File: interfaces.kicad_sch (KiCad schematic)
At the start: 87 parts, among them IC3 TPD8S009DSMR, J5 HDMI-A_685119134923, J6 USB_Micro-B_629105150521, J7 MicroSD_1140084168, Q3 BSS138PW, Q4 BSS138PW, Q5 BSS138PW, Q6 BSS138PW, Q7 BSS138PW, U10 FT4232H_QFN, Y2 Oscillator_SMD_12MHz_KX-7

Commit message: [#80386] Add company name in board settings
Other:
- company: Antmicro Ltd. -> Antmicro
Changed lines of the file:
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@@
 		(date "2023-07-27")
 		(rev "1.0.1")
-		(company "Antmicro Ltd.")
+		(company "Antmicro")
 		(comment 1 "www.antmicro.com")
-		(comment 2 "Antmicro Ltd")
 	)
 	(text "Debug USB"

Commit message: [#87036] Update components, clear DRC and ERC
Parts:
- removed IC3: TPD8S009DSMR, data-center-rdimm-ddr5-tester-footprints:R-PDSO-N15, symbol data-center-rdimm-ddr5-tester:TPD8S009DSMR
- added IC3: TPD8S009DSMR, antmicro-footprints:R-PDSO-N15, symbol antmicroTVSDiodes:TPD8S009DSMR
- C148, C149, C154, C156, C157, C158, C159, C160, C161, C162: footprint data-center-rdimm-ddr5-tester-footprints:C_0402_1005Metric -> antmicro-footprints:C_0402_1005Metric; symbol data-center-rdimm-ddr5-tester:C_100n_6V3_0402 -> antmicroCapacitorsmisc:C_100n_6V3_0402; Public (none) -> False
- C150, C152, C155: footprint data-center-rdimm-ddr5-tester-footprints:C_0402_1005Metric -> antmicro-footprints:C_0402_1005Metric; symbol data-center-rdimm-ddr5-tester:C_4u7_0402 -> antmicroCapacitors0402:C_4u7_0402
- C151, C153: footprint data-center-rdimm-ddr5-tester-footprints:C_0402_1005Metric -> antmicro-footprints:C_0402_1005Metric; symbol data-center-rdimm-ddr5-tester:C_18p_0402 -> antmicroCapacitors0402:C_18p_0402; MPN MC0402N180J500CT -> CL05C180JB51PNC; Manufacturer Multicomp -> Samsung Electro-Mechanics
- C163: footprint data-center-rdimm-ddr5-tester-footprints:C_0603_1608Metric -> antmicro-footprints:C_0603_1608Metric; symbol data-center-rdimm-ddr5-tester:C_1u_0603 -> antmicroCapacitors0603:C_1u_0603; Manufacturer Walsin -> KYOCERA AVX
- D10, D11, D7, D8, D9: footprint data-center-rdimm-ddr5-tester-footprints:LED_0603_1608Metric_G -> antmicro-footprints:LED_0603_1608Metric_G; symbol data-center-rdimm-ddr5-tester:LED_G_0603_KP-1608CGCK -> antmicroLEDIndicationDiscrete:LED_G_0603_KP-1608CGCK; Color (none) -> Green
- D12: footprint data-center-rdimm-ddr5-tester-footprints:SOT-723 -> antmicro-footprints:SOT-723; symbol data-center-rdimm-ddr5-tester:TPD2E009_SOT-9X3 -> antmicroTVSDiodes:TPD2E009_SOT-9X3
- FB5, FB6, FB8: footprint data-center-rdimm-ddr5-tester-footprints:FB_0603_1608Metric -> antmicro-footprints:FB_0603_1608Metric; symbol data-center-rdimm-ddr5-tester:FB_600Z_0.5A_0603 -> antmicroFerriteBeadsandChips:FB_600Z_0.5A_Murata-BLM18AG_0603; Val (none) -> 600Z/0.5A
- FB7: footprint data-center-rdimm-ddr5-tester-footprints:FB_0603_1608Metric -> antmicro-footprints:FB_0603_1608Metric; symbol data-center-rdimm-ddr5-tester:FB_120Z_2A_0603 -> antmicroFerriteBeadsandChips:FB_120Z_2A_Murata-BLM18PG_0603; Val (none) -> 120Z/2A
- J5: footprint data-center-rdimm-ddr5-tester-footprints:HDMI-A_Wurth_685119134923 -> antmicro-footprints:HDMI-A_Receptacle_WE_685119134923; symbol data-center-rdimm-ddr5-tester:HDMI-A_685119134923 -> antmicroVideoConnectors:HDMI-A_WE_685119134923; Manufacturer Wurth Electronic -> Würth Elektronik
- J6: footprint data-center-rdimm-ddr5-tester-footprints:USB_Micro_B_Female_629105150521 -> antmicro-footprints:USB-Micro-B_Receptacle_WE_629105150521; symbol data-center-rdimm-ddr5-tester:USB_Micro-B_629105150521 -> antmicroUSBConnectors:USB-Micro-B_WE_629105150521; Manufacturer Wurth_Elektronik -> Würth Elektronik
- J7: footprint data-center-rdimm-ddr5-tester-footprints:MicroSD_Amphenol_1140084168 -> antmicro-footprints:MicroSD_Amphenol_1140084168; symbol data-center-rdimm-ddr5-tester:MicroSD_1140084168 -> antmicroMemoryConnectorsPCCardSockets:MicroSD_1140084168
- PROG_B2, PROG_B3, PROG_B4, PROG_B5: footprint data-center-rdimm-ddr5-tester-footprints:SW_B3U-3000P -> antmicro-footprints:SW_B3U-1000P_SMD; symbol data-center-rdimm-ddr5-tester:SW_B3U-1000P -> antmicroPushbuttonSwitches:SW_B3U-1000P_SMD; Manufacturer Omron Electronics -> Omron
- Q3, Q4, Q5, Q6, Q7: footprint data-center-rdimm-ddr5-tester-footprints:SC70-3 -> antmicro-footprints:SC70-3; symbol data-center-rdimm-ddr5-tester:BSS138PW -> antmicroTransistorsFETsMOSFETsSingle:BSS138PW
- R100, R88, R89, R90, R91, R92, R93, R94, R95, R96, R97, R98, R99: footprint data-center-rdimm-ddr5-tester-footprints:R_0402_1005Metric -> antmicro-footprints:R_0402_1005Metric; symbol data-center-rdimm-ddr5-tester:R_22R_0402 -> antmicroResistors0402:R_22R_0402
- R101, R102, R103, R104, R105: footprint data-center-rdimm-ddr5-tester-footprints:R_0402_1005Metric -> antmicro-footprints:R_0402_1005Metric; symbol data-center-rdimm-ddr5-tester:R_330R_0402 -> antmicroResistors0402:R_330R_0402
- R106, R107, R109, R111, R113, R116, R118: footprint data-center-rdimm-ddr5-tester-footprints:R_0402_1005Metric -> antmicro-footprints:R_0402_1005Metric; symbol data-center-rdimm-ddr5-tester:R_20k_0402 -> antmicroResistors0402:R_20k_0402
- R108, R110, R112, R115, R117, R119, R120, R121: footprint data-center-rdimm-ddr5-tester-footprints:R_0402_1005Metric -> antmicro-footprints:R_0402_1005Metric; symbol data-center-rdimm-ddr5-tester:R_0R_0402 -> antmicroResistors0402:R_0R_0402
- R114: footprint data-center-rdimm-ddr5-tester-footprints:R_0402_1005Metric -> antmicro-footprints:R_0402_1005Metric; symbol data-center-rdimm-ddr5-tester:R_220R_0402 -> antmicroResistors0402:R_220R_0402
- R82, R83, R84, R85: footprint data-center-rdimm-ddr5-tester-footprints:R_0402_1005Metric -> antmicro-footprints:R_0402_1005Metric; symbol data-center-rdimm-ddr5-tester:R_4k7_0402 -> antmicroResistors0402:R_4k7_0402
- R86: footprint data-center-rdimm-ddr5-tester-footprints:R_0402_1005Metric -> antmicro-footprints:R_0402_1005Metric; symbol data-center-rdimm-ddr5-tester:R_12k_0402 -> antmicroResistors0402:R_12k_0402
- R87: footprint data-center-rdimm-ddr5-tester-footprints:R_0402_1005Metric -> antmicro-footprints:R_0402_1005Metric; symbol data-center-rdimm-ddr5-tester:R_10k_0402 -> antmicroResistors0402:R_10k_0402
- TP10, TP5, TP6, TP7, TP8, TP9: footprint data-center-rdimm-ddr5-tester-footprints:Testpoint_smd_1mm -> antmicro-footprints:TP_SMD_1mm; symbol data-center-rdimm-ddr5-tester:TP_1mm_SMD -> antmicroTestPoints:TP_1mm_SMD
- U10: footprint data-center-rdimm-ddr5-tester-footprints:QFN-64_1EP_9x9mm_P0.5mm -> antmicro-footprints:QFN-64-1EP_9x9mm_P0.5mm; symbol data-center-rdimm-ddr5-tester:FT4232H_QFN -> antmicroInterfaceControllers:FT4232H_QFN; Manufacturer FTDI -> FTDI Chip
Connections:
- net C_TMDS_CLK_N: now also IC3.12 (D3-)
- net C_TMDS_CLK_P: now also IC3.10 (D3+)
- net C_TMDS_D0_N: now also IC3.9 (D2-)
- net C_TMDS_D0_P: now also IC3.7 (D2+)
- net C_TMDS_D1_N: now also IC3.6 (D1-)
- net C_TMDS_D1_P: now also IC3.4 (D1+)
- net C_TMDS_D2_N: now also IC3.3 (D0-)
- net C_TMDS_D2_P: now also IC3.1 (D0+)
- net GND: now also IC3.11 (GND), IC3.2 (GND), IC3.5 (GND), IC3.8 (GND)
- net at R101.1: now also D7.1 (C); no longer D7.2
- net at FB8.2: now also J6.SH (SHIELD); no longer J6.6
- net at R103.1: now also D9.1 (C); no longer D9.2
- net at R104.1: now also D10.1 (C); no longer D10.2
- net at R105.1: now also D11.1 (C); no longer D11.2
- net at R102.1: now also D8.1 (C); no longer D8.2
- net 1V8_SYS renamed +1V8
- net 3V3_SYS renamed +3V3
- net +3V3: now also D10.2 (A), D11.2 (A), D7.2 (A), D8.2 (A), D9.2 (A), IC3.13 (VCC), IC3.15 (VCC); no longer D10.1, D11.1, D7.1, D8.1, D9.1
- net VBUS: no longer names the net of J6.1 (VBUS)
- no-connect marks 26 -> 27
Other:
- moved on the sheet: C148, C150, C151, C153, C154, C155, C156, C157, C158, C159, C160, C161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

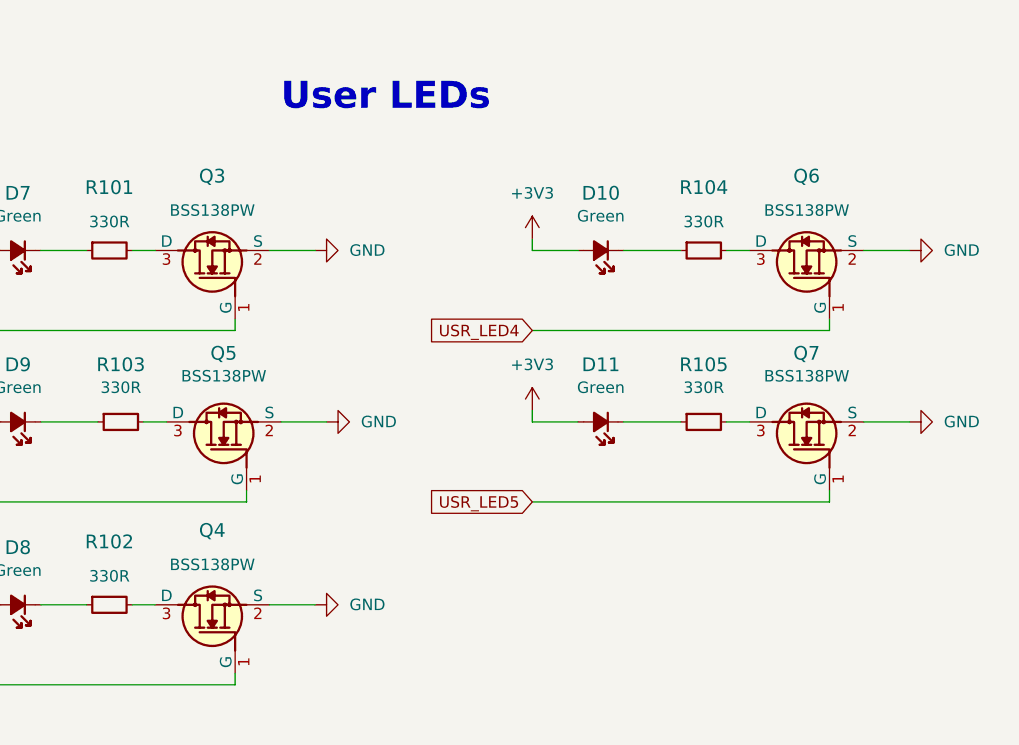
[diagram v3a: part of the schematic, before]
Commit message: [#87036] Update BSS138 transistors
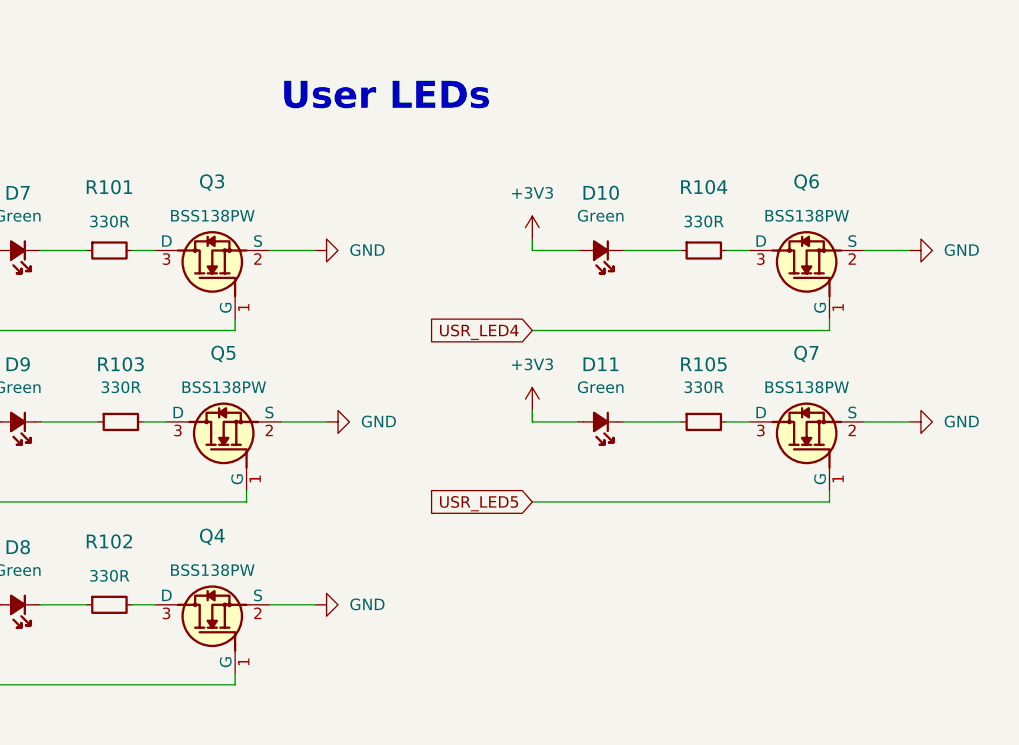
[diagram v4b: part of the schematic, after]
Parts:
- Q3, Q4, Q5, Q6, Q7: symbol antmicroTransistorsFETsMOSFETsSingle:BSS138PW -> antmicroTransistorsFETsMOSFETsSingle:BSS138PW,115; MPN BSS138PW -> BSS138PW,115
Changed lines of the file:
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@@
 	)
 	(symbol
-		(lib_id "antmicroTransistorsFETsMOSFETsSingle:BSS138PW")
+		(lib_id "antmicroTransistorsFETsMOSFETsSingle:BSS138PW,115")
 		(at 177.8 229.87 90)
 		(unit 1)
@@
 		(fields_autoplaced yes)
 		(property "Reference" "Q3"
-			(at 175.26 213.995 90)
+			(at 175.26 214.63 90)
 			(effects
 				(font
@@
 		)
 		(property "Value" "BSS138PW"
-			(at 175.26 217.805 90)
+			(at 175.26 218.44 90)
 			(effects
 				(font
@@
 		)
 		(property "Description" "Power MOSFET, N Channel, 60 V, 320 mA, 0.9 ohm, SOT-323, Surface Mount"
-			(at 177.8 229.87 0)
-			(effects
-				(font
-					(size 1.27 1.27)
-				)
-				(hide yes)
-			)
-		)
-		(property "MPN" "BSS138PW"
-			(at 194.31 207.01 0)
-			(effects
-				(font
-					(size 1.27 1.27)
-					(thickness 0.15)
-				)
-				(justify left bottom)
+			(at 204.47 207.01 0)
+			(effects
+				(font
+					(size 1.27 1.27)
+				)
+				(justify left bottom)
+				(hide yes)
+			)
+		)
+		(property "MPN" "BSS138PW,115"
+			(at 175.26 218.44 90)
+			(effects
+				(font
+					(size 1.27 1.27)
+					(thickness 0.15)
+				)
 				(hide yes)
 			)
@@
 	)
 	(symbol
-		(lib_id "antmicroTransistorsFETsMOSFETsSingle:BSS138PW")
+		(lib_id "antmicroTransistorsFETsMOSFETsSingle:BSS138PW,115")
 		(at 179.07 248.92 90)
 		(unit 1)
@@
 		)
 		(property "Value" "BSS138PW"
-			(at 176.53 236.22 90)
+			(at 176.53 237.49 90)
 			(effects
 				(font
@@
 		)
 		(property "Description" "Power MOSFET, N Channel, 60 V, 320 mA, 0.9 ohm, SOT-323, Surface Mount"
-			(at 179.07 248.92 0)
-			(effects
-				(font
-					(size 1.27 1.27)
-				)
-				(hide yes)
-			)
-		)
-		(property "MPN" "BSS138PW"
-			(at 195.58 226.06 0)
-			(effects
-				(font
-					(size 1.27 1.27)
-					(thickness 0.15)
-				)
-				(justify left bottom)
+			(at 205.74 226.06 0)
+			(effects
+				(font
+					(size 1.27 1.27)
+				)
+				(justify left bottom)
+				(hide yes)
+			)
+		)
+		(property "MPN" "BSS138PW,115"
+			(at 176.53 237.49 90)
+			(effects
+				(font
+					(size 1.27 1.27)
+					(thickness 0.15)
+				)
 				(hide yes)
 			)
@@
 	)
 	(symbol
-		(lib_id "antmicroTransistorsFETsMOSFETsSingle:BSS138PW")
+		(lib_id "antmicroTransistorsFETsMOSFETsSingle:BSS138PW,115")
 		(at 243.84 229.87 90)
 		(unit 1)
@@
 		(fields_autoplaced yes)
 		(property "Reference" "Q6"
-			(at 241.3 213.995 90)
+			(at 241.3 214.63 90)
 			(effects
 				(font
@@
 		)
 		(property "Value" "BSS138PW"
-			(at 241.3 217.805 90)
+			(at 241.3 218.44 90)
 			(effects
 				(font
@@
 		)
 		(property "Description" "Power MOSFET, N Channel, 60 V, 320 mA, 0.9 ohm, SOT-323, Surface Mount"
-			(at 243.84 229.87 0)
-			(effects
-				(font
-					(size 1.27 1.27)
-				)
-				(hide yes)
-			)
-		)
-		(property "MPN" "BSS138PW"
-			(at 260.35 207.01 0)
-			(effects
-				(font
-					(size 1.27 1.27)
-					(thickness 0.15)
-				)
-				(justify left bottom)
+			(at 270.51 207.01 0)
+			(effects
+				(font
+					(size 1.27 1.27)
+				)
+				(justify left bottom)
+				(hide yes)
+			)
+		)
+		(property "MPN" "BSS138PW,115"
+			(at 241.3 218.44 90)
+			(effects
+				(font
+					(size 1.27 1.27)
+					(thickness 0.15)
+				)
 				(hide yes)
 			)
@@
 	)
 	(symbol
-		(lib_id "antmicroTransistorsFETsMOSFETsSingle:BSS138PW")
+		(lib_id "antmicroTransistorsFETsMOSFETsSingle:BSS138PW,115")
 		(at 243.84 248.92 90)
 		(unit 1)
@@
 		)
 		(property "Value" "BSS138PW"
-			(at 241.3 236.22 90)
+			(at 241.3 237.49 90)
 			(effects
 				(font
@@
 		)
 		(property "Description" "Power MOSFET, N Channel, 60 V, 320 mA, 0.9 ohm, SOT-323, Surface Mount"
-			(at 243.84 248.92 0)
-			(effects
-				(font
-					(size 1.27 1.27)
-				)
-				(hide yes)
-			)
-		)
-		(property "MPN" "BSS138PW"
-			(at 260.35 226.06 0)
-			(effects
-				(font
-					(size 1.27 1.27)
-					(thickness 0.15)
-				)
-				(justify left bottom)
+			(at 270.51 226.06 0)
+			(effects
+				(font
+					(size 1.27 1.27)
+				)
+				(justify left bottom)
+				(hide yes)
+			)
+		)
+		(property "MPN" "BSS138PW,115"
+			(at 241.3 237.49 90)
+			(effects
+				(font
+					(size 1.27 1.27)
+					(thickness 0.15)
+				)
 				(hide yes)
 			)
@@
 	)
 	(symbol
-		(lib_id "antmicroTransistorsFETsMOSFETsSingle:BSS138PW")
+		(lib_id "antmicroTransistorsFETsMOSFETsSingle:BSS138PW,115")
 		(at 177.8 269.24 90)
 		(unit 1)
@@
 		(fields_autoplaced yes)
 		(property "Reference" "Q4"
-			(at 175.26 253.365 90)
+			(at 175.26 254 90)
 			(effects
 				(font
@@
 		)
 		(property "Value" "BSS138PW"
-			(at 175.26 257.175 90)
+			(at 175.26 257.81 90)
 			(effects
 				(font
@@
 		)
 		(property "Description" "Power MOSFET, N Channel, 60 V, 320 mA, 0.9 ohm, SOT-323, Surface Mount"
-			(at 177.8 269.24 0)
-			(effects
-				(font
-					(size 1.27 1.27)
-				)
-				(hide yes)
-			)
-		)
-		(property "MPN" "BSS138PW"
-			(at 194.31 246.38 0)
-			(effects
-				(font
-					(size 1.27 1.27)
-					(thickness 0.15)
-				)
-				(justify left bottom)
-				(hide yes)
-			)
+			(at 204.47 246.38 0)
+			(effects
+				(font
+					(size 1.27 1.27)
+				)
+				(justify left bottom)
+				(hide yes)
+			)
+		)
+		(property "MPN" "BSS138PW,115"
+			(at 175.26 257.81 90)
+			(effects
+				(font
+					(size 1.27 1.27)
+					(thickness 0.15)
+				)
+				(hide yes)
+			)

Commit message: [#87036] Add EEPROM with unique ID
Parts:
- added C239: C_100n_0402, antmicro-footprints:C_0402_1005Metric, symbol antmicroCapacitors0402:C_100n_0402
- added D17, D18: BAT54-02V-G3-08, antmicro-footprints:SOD-523, symbol antmicroDiodesRectifiersSingle:BAT54-02V-G3-08
- added R19, R21: R_0R_0402, antmicro-footprints:R_0402_1005Metric, symbol antmicroResistors0402:R_0R_0402
- added TP67, TP68, TP69, TP70: TP_1mm_SMD, antmicro-footprints:TP_SMD_1mm, symbol antmicroTestPoints:TP_1mm_SMD
- added U34: AT24CS01_SOT23, antmicro-footprints:SOT-23-5, symbol antmicroMemory:AT24CS01_SOT23
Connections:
- net +3V3: now also D17.2 (A)
- net GND: now also C239.1, TP68.1, U34.2 (GND), U34.5 (WP)
- new net: C239.2, D17.1 (C), D18.1 (C), U34.4 (VCC)
- new net: D18.2 (A), TP67.1
- new net: R21.2, TP70.1, U34.1 (SCL)
- new net: R19.2, TP69.1, U34.3 (SDA)
- new net SCL_3V3: R21.1
- new net SDA_3V3: R19.1
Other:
- note added: "UID EEPROM"
